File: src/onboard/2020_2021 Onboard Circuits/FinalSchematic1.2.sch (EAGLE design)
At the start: 78 parts, among them IC1 MIC2937A-5.0BT, IC3 A5975D

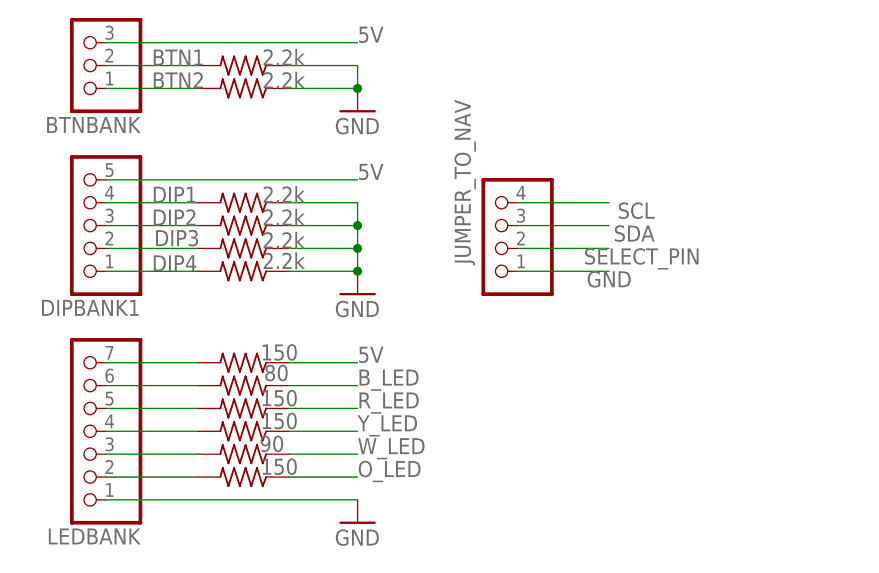
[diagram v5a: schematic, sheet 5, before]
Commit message: Added pulldown on select pin and added wiring for aux pin
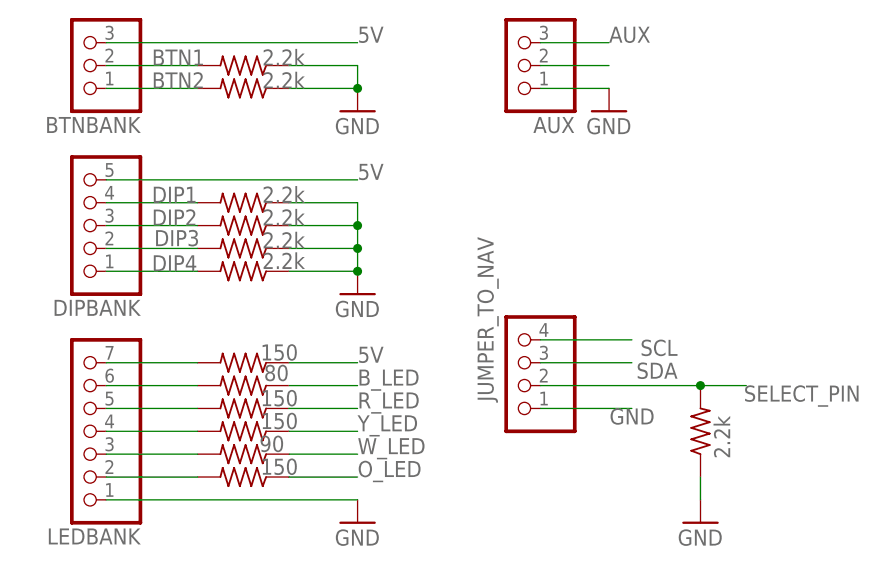
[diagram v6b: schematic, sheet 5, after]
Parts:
- removed AUX_DATA: (no value), pinhead:PINHD-1X1
- added AUX: (no value), pinhead:PINHD-1X3
- added R23: 2.2k, adafruit:R-US_0204/7
- renumbered DIPBANK1 to DIPBANK
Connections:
- new net AUX: AUX.3, TEENSY4.1.27-A13/SCK1
- new net N$4: AUX.2
- net AUX_DATA: no longer AUX_DATA.1
- net GND: now also AUX.1, R23.1
- net SELECT_PIN: now also R23.2
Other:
- moved on the sheet: JUMPER_TO_NAV
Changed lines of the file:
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@@
 <part name="GND6" library="supply1" library_urn="urn:adsk.eagle:library:371" deviceset="GND" device=""/>
 <part name="L2" library="rcl" library_urn="urn:adsk.eagle:library:334" deviceset="L-US" device="TFI0307" package3d_urn="urn:adsk.eagle:package:23534/1" value="27uH"/>
-<part name="AUX_DATA" library="pinhead" library_urn="urn:adsk.eagle:library:325" deviceset="PINHD-1X1" device="" package3d_urn="urn:adsk.eagle:package:22485/2"/>
 <part name="JUMPER_TO_NAV" library="pinhead" library_urn="urn:adsk.eagle:library:325" deviceset="PINHD-1X4" device="" package3d_urn="urn:adsk.eagle:package:22407/2"/>
 <part name="ORANGE" library="adafruit" library_urn="urn:adsk.eagle:library:420" deviceset="R-US_" device="0204/7" package3d_urn="urn:adsk.eagle:package:6240596/1" value="150"/>
@@
 <part name="GND10" library="supply1" library_urn="urn:adsk.eagle:library:371" deviceset="GND" device=""/>
 <part name="BTNBANK" library="pinhead" library_urn="urn:adsk.eagle:library:325" deviceset="PINHD-1X3" device="" package3d_urn="urn:adsk.eagle:package:22458/2"/>
-<part name="DIPBANK1" library="pinhead" library_urn="urn:adsk.eagle:library:325" deviceset="PINHD-1X5" device="" package3d_urn="urn:adsk.eagle:package:22469/2"/>
+<part name="DIPBANK" library="pinhead" library_urn="urn:adsk.eagle:library:325" deviceset="PINHD-1X5" device="" package3d_urn="urn:adsk.eagle:package:22469/2"/>
 <part name="GND11" library="supply1" library_urn="urn:adsk.eagle:library:371" deviceset="GND" device=""/>
 <part name="6V_PWR" library="pinhead" library_urn="urn:adsk.eagle:library:325" deviceset="PINHD-1X3" device="" package3d_urn="urn:adsk.eagle:package:22458/2"/>
@@
 <part name="GND8" library="supply1" library_urn="urn:adsk.eagle:library:371" deviceset="GND" device=""/>
 <part name="C1" library="capacitor-wima" library_urn="urn:adsk.eagle:library:116" deviceset="C" device="2,5-3" package3d_urn="urn:adsk.eagle:package:5436/1" value="10uF"/>
+<part name="R23" library="adafruit" library_urn="urn:adsk.eagle:library:420" deviceset="R-US_" device="0204/7" package3d_urn="urn:adsk.eagle:package:6240596/1" value="2.2k"/>
+<part name="GND9" library="supply1" library_urn="urn:adsk.eagle:library:371" deviceset="GND" device=""/>
+<part name="AUX" library="pinhead" library_urn="urn:adsk.eagle:library:325" deviceset="PINHD-1X3" device="" package3d_urn="urn:adsk.eagle:package:22458/2"/>
+<part name="GND12" library="supply1" library_urn="urn:adsk.eagle:library:371" deviceset="GND" device=""/>
 </parts>
 <sheets>
@@
 </segment>
 </net>
+<net name="AUX" class="0">
+<segment>
+<pinref part="TEENSY4.1" gate="G$1" pin="27-A13/SCK1"/>
+<wire x1="34.29" y1="48.26" x2="30.48" y2="48.26" width="0.1524" layer="91"/>
+<label x="27.94" y="48.26" size="1.778" layer="95"/>
+</segment>
+</net>
 </nets>
 </sheet>
@@
 <attribute name="VALUE" x="29.21" y="68.58" size="1.778" layer="96" rot="R180"/>
 </instance>
-<instance part="DIPBANK1" gate="A" x="22.86" y="43.18" smashed="yes" rot="R180">
+<instance part="DIPBANK" gate="A" x="22.86" y="43.18" smashed="yes" rot="R180">
 <attribute name="NAME" x="29.21" y="34.925" size="1.778" layer="95" rot="R180"/>
 <attribute name="VALUE" x="29.21" y="53.34" size="1.778" layer="96" rot="R180"/>
@@
 <attribute name="VALUE" x="50.8" y="7.62" size="1.778" layer="96"/>
 </instance>
-<instance part="JUMPER_TO_NAV" gate="A" x="68.58" y="43.18" smashed="yes" rot="R180">
-<attribute name="NAME" x="64.135" y="57.15" size="1.778" layer="95" rot="R270"/>
-<attribute name="VALUE" x="74.93" y="50.8" size="1.778" layer="96" rot="R180"/>
+<instance part="JUMPER_TO_NAV" gate="A" x="71.12" y="27.94" smashed="yes" rot="R180">
+<attribute name="NAME" x="66.675" y="41.91" size="1.778" layer="95" rot="R270"/>
+<attribute name="VALUE" x="77.47" y="35.56" size="1.778" layer="96" rot="R180"/>
+</instance>
+<instance part="R23" gate="G$1" x="91.44" y="20.32" smashed="yes" rot="R90">
+<attribute name="VALUE" x="94.742" y="17.272" size="1.778" layer="96" rot="R90"/>
+</instance>
+<instance part="GND9" gate="1" x="91.44" y="10.16" smashed="yes">
+<attribute name="VALUE" x="88.9" y="7.62" size="1.778" layer="96"/>
+</instance>
+<instance part="AUX" gate="A" x="71.12" y="60.96" smashed="yes" rot="R180">
+<attribute name="NAME" x="77.47" y="55.245" size="1.778" layer="95" rot="R180"/>
+<attribute name="VALUE" x="77.47" y="68.58" size="1.778" layer="96" rot="R180"/>
+</instance>
+<instance part="GND12" gate="1" x="81.28" y="55.88" smashed="yes">
+<attribute name="VALUE" x="78.74" y="53.34" size="1.778" layer="96"/>
 </instance>
 </instances>
@@
 <wire x1="25.4" y1="48.26" x2="53.34" y2="48.26" width="0.1524" layer="91"/>
 <label x="53.34" y="48.26" size="1.778" layer="95"/>
-<pinref part="DIPBANK1" gate="A" pin="5"/>
+<pinref part="DIPBANK" gate="A" pin="5"/>
 </segment>
 <segment>
@@
 <pinref part="R37" gate="G$1" pin="2"/>
 <label x="30.48" y="45.72" size="1.778" layer="95"/>
-<pinref part="DIPBANK1" gate="A" pin="4"/>
+<pinref part="DIPBANK" gate="A" pin="4"/>
 </segment>
 </net>
@@
 <pinref part="R35" gate="G$1" pin="2"/>
 <label x="30.48" y="38.1" size="1.778" layer="95"/>
-<pinref part="DIPBANK1" gate="A" pin="1"/>
+<pinref part="DIPBANK" gate="A" pin="1"/>
 </segment>
 </net>
@@
 <pinref part="R36" gate="G$1" pin="2"/>
 <label x="30.48" y="43.18" size="1.778" layer="95"/>
-<pinref part="DIPBANK1" gate="A" pin="3"/>
+<pinref part="DIPBANK" gate="A" pin="3"/>
 </segment>
 </net>
@@
 <pinref part="R34" gate="G$1" pin="2"/>
 <label x="30.734" y="40.894" size="1.778" layer="95"/>
-<pinref part="DIPBANK1" gate="A" pin="2"/>
+<pinref part="DIPBANK" gate="A" pin="2"/>
 </segment>
 </net>
@@
 <segment>
 <pinref part="JUMPER_TO_NAV" gate="A" pin="1"/>
-<wire x1="71.12" y1="38.1" x2="81.28" y2="38.1" width="0.1524" layer="91"/>
-<label x="83.82" y="38.1" size="1.778" layer="95" rot="R180"/>
+<wire x1="73.66" y1="22.86" x2="83.82" y2="22.86" width="0.1524" layer="91"/>
+<label x="86.36" y="22.86" size="1.778" layer="95" rot="R180"/>
+</segment>
+<segment>
+<pinref part="R23" gate="G$1" pin="1"/>
+<pinref part="GND9" gate="1" pin="GND"/>
+<wire x1="91.44" y1="15.24" x2="91.44" y2="12.7" width="0.1524" layer="91"/>
+</segment>
+<segment>
+<pinref part="AUX" gate="A" pin="1"/>
+<wire x1="73.66" y1="58.42" x2="81.28" y2="58.42" width="0.1524" layer="91"/>
+<pinref part="GND12" gate="1" pin="GND"/>
 </segment>
 </net>
@@
 <segment>
 <pinref part="JUMPER_TO_NAV" gate="A" pin="3"/>
-<wire x1="71.12" y1="43.18" x2="81.28" y2="43.18" width="0.1524" layer="91"/>
-<label x="86.36" y="43.18" size="1.778" layer="95" rot="R180"/>
+<wire x1="73.66" y1="27.94" x2="83.82" y2="27.94" width="0.1524" layer="91"/>
+<label x="88.9" y="27.94" size="1.778" layer="95" rot="R180"/>
 </segment>
 </net>
@@
 <segment>
 <pinref part="JUMPER_TO_NAV" gate="A" pin="4"/>
-<wire x1="71.12" y1="45.72" x2="81.28" y2="45.72" width="0.1524" layer="91"/>
-<label x="86.36" y="45.72" size="1.778" layer="95" rot="R180"/>
+<wire x1="73.66" y1="30.48" x2="83.82" y2="30.48" width="0.1524" layer="91"/>
+<label x="88.9" y="30.48" size="1.778" layer="95" rot="R180"/>
 </segment>
 </net>
@@
 <segment>
 <pinref part="JUMPER_TO_NAV" gate="A" pin="2"/>
-<wire x1="71.12" y1="40.64" x2="81.28" y2="40.64" width="0.1524" layer="91"/>
-<label x="91.44" y="40.64" size="1.778" layer="95" rot="R180"/>
+<wire x1="73.66" y1="25.4" x2="91.44" y2="25.4" width="0.1524" layer="91"/>
+<label x="109.22" y="25.4" size="1.778" layer="95" rot="R180"/>
+<pinref part="R23" gate="G$1" pin="2"/>
+<wire x1="91.44" y1="25.4" x2="96.52" y2="25.4" width="0.1524" layer="91"/>
+<junction x="91.44" y="25.4"/>
+</segment>
+</net>
+<net name="N$4" class="0">
+<segment>
+<pinref part="AUX" gate="A" pin="2"/>
+<wire x1="73.66" y1="60.96" x2="81.28" y2="60.96" width="0.1524" layer="91"/>
+</segment>
+</net>
+<net name="AUX" class="0">
+<segment>
+<pinref part="AUX" gate="A" pin="3"/>
+<wire x1="73.66" y1="63.5" x2="81.28" y2="63.5" width="0.1524" layer="91"/>
+<label x="81.28" y="63.5" size="1.778" layer="95"/>
 </segment>
 </net>
@@
 </plain>
 <instances>
-<instance part="AUX_DATA" gate="G$1" x="60.96" y="68.58" smashed="yes" rot="R90">
-<attribute name="NAME" x="67.31" y="73.025" size="1.778" layer="95" rot="R180"/>
-<attribute name="VALUE" x="66.04" y="62.23" size="1.778" layer="96" rot="R90"/>
-</instance>
 <instance part="TP1" gate="G$1" x="12.7" y="50.8" smashed="yes" rot="R270">
 <attribute name="NAME" x="6.35" y="51.816" size="1.778" layer="95"/>
@@
 </segment>
 </net>
-<net name="AUX_DATA" class="0">
-<segment>
-<pinref part="AUX_DATA" gate="G$1" pin="1"/>
-<wire x1="60.96" y1="66.04" x2="60.96" y2="60.96" width="0.1524" layer="91"/>
-<label x="66.04" y="60.96" size="1.778" layer="95" rot="R180"/>
-</segment>
-</net>
